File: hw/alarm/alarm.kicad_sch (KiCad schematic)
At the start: 64 parts, among them IC3 SHT40-BD1B-R2, IC5 PEC11S-929K-S0015, IC6 MAX31328NELB+, J1 4328, J2 FFC2B35-24-T, J3 975, Q1 DMG2305UX-7, Q2 2SC5585TL, Q3 Si1308EDL-T1-GE3, Q4 DMG2305UX-7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

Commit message: Finish most of board layout
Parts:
- removed S7: DS01-254-L-01BE, DS01254L01BE, symbol SamacSys_Parts:DS01-254-L-01BE
- added S7: RKB2SJK250SMTR_LFS, RKB2SJK250SMTRLFS, symbol SamacSys_Parts:RKB2SJK250SMTR_LFS
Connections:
- net +3.3V: now also S7.2 (COM_2)
- net Buzzer: now also U1.4 (GPIO2); no longer U1.20 (GPIO15)
- net EinkBUSY: now also U1.21 (GPIO16); no longer U1.22 (GPIO17)
- net EinkCS: now also U1.29 (GPIO22); no longer U1.10 (GPIO7)
- net EinkRESET: now also U1.22 (GPIO17); no longer U1.21 (GPIO16)
- net Enc_A1: now also U1.2 (GPIO1); no longer U1.11 (GPIO8)
- net Enc_B1: now also U1.1 (GPIO0); no longer U1.12 (GPIO9)
- net RF1: now also U1.20 (GPIO15); no longer U1.5 (GPIO3)
- net MISO: no longer names the net of U1.26 (GPIO20)
- net RF_key: no longer names the net of A1.7 (KEY), R15.2, R3.1
- net RF_key: now also S7.4 (NO_2); no longer U1.4 (GPIO2)
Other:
- note added: "Qwiic"
- note removed: "Stemma-QT"
- moved on the sheet: J1, R5, R6

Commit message: Finish board layout pending last checks
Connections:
- net GND: now also J3.3 (-); no longer J3.1 (-)
- net at Q4.3 (D): now also J3.1 (+); no longer J3.3 (+)
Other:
- moved on the sheet: J3
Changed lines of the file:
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@@
 	(wire
 		(pts
-			(xy 191.77 73.66) (xy 184.15 73.66)
-		)
-		(stroke
-			(width 0)
-			(type default)
-		)
-	)
-	(wire
-		(pts
 			(xy 396.24 175.26) (xy 403.86 175.26)
 		)
@@
 	(wire
 		(pts
-			(xy 191.77 73.66) (xy 191.77 74.93)
+			(xy 158.75 73.66) (xy 173.99 73.66)
 		)
 		(stroke
@@
 	(wire
 		(pts
-			(xy 186.69 278.13) (xy 194.31 278.13)
+			(xy 179.07 73.66) (xy 179.07 74.93)
 		)
 		(stroke
@@
 	(wire
 		(pts
-			(xy 179.07 73.66) (xy 179.07 74.93)
+			(xy 186.69 278.13) (xy 194.31 278.13)
 		)
 		(stroke
@@
 	(symbol
 		(lib_id "SamacSys_Parts:975")
-		(at 179.07 73.66 90)
+		(at 173.99 73.66 90)
 		(unit 1)
 		(exclude_from_sim no)
@@
 		(fields_autoplaced yes)
 		(property "Reference" "J3"
-			(at 187.96 62.2299 90)
+			(at 182.88 62.2299 90)
 			(effects
 				(font
@@
 		)
 		(property "Value" "975"
-			(at 187.96 64.7699 90)
+			(at 182.88 64.7699 90)
 			(effects
 				(font
@@
 		)
 		(property "Footprint" "975"
-			(at 273.99 57.15 0)
+			(at 268.91 57.15 0)
 			(effects
 				(font
@@
 		)
 		(property "Datasheet" "https://componentsearchengine.com/Datasheets/1/975.pdf"
-			(at 373.99 57.15 0)
+			(at 368.91 57.15 0)
 			(effects
 				(font
@@
 		)
 		(property "Description" "Headers & Wire Housings WIRE TO BOARD THM CONN, 3 TERM, VERT"
-			(at 179.07 73.66 0)
+			(at 173.99 73.66 0)
 			(effects
 				(font
@@
 		)
 		(property "Height" "7.7"
-			(at 573.99 57.15 0)
+			(at 568.91 57.15 0)
 			(effects
 				(font
@@
 		)
 		(property "Mouser Part Number" "534-975"
-			(at 673.99 57.15 0)
+			(at 668.91 57.15 0)
 			(effects
 				(font
@@
 		)
 		(property "Mouser Price/Stock" "https://www.mouser.co.uk/ProductDetail/Keystone-Electronics/975?qs=5aG0NVq1C4xEu03Xxaum1g%3D%3D"
-			(at 773.99 57.15 0)
+			(at 768.91 57.15 0)
 			(effects
 				(font
@@
 		)
 		(property "Manufacturer_Name" "Keystone Electronics"
-			(at 873.99 57.15 0)
+			(at 868.91 57.15 0)
 			(effects
 				(font
@@
 		)
 		(property "Manufacturer_Part_Number" "975"
-			(at 973.99 57.15 0)
+			(at 968.91 57.15 0)
 			(effects
 				(font
@@
 	(symbol
 		(lib_id "power:GND")
-		(at 191.77 74.93 0)
+		(at 158.75 73.66 270)
 		(unit 1)
 		(exclude_from_sim no)
@@
 		(fields_autoplaced yes)
 		(property "Reference" "#PWR019"
-			(at 191.77 81.28 0)
+			(at 152.4 73.66 0)
 			(effects
 				(font
@@
 		)
 		(property "Value" "GND"
-			(at 191.77 80.01 0)
+			(at 153.67 73.66 0)
 			(effects
 				(font
@@
 		)
 		(property "Footprint" ""
-			(at 191.77 74.93 0)
+			(at 158.75 73.66 0)
 			(effects
 				(font
@@
 		)
 		(property "Datasheet" ""
-			(at 191.77 74.93 0)
+			(at 158.75 73.66 0)
 			(effects
 				(font
@@
 		)
 		(property "Description" "Power symbol creates a global label with name \"GND\" , ground"
-			(at 191.77 74.93 0)
+			(at 158.75 73.66 0)
 			(effects
 				(font

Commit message: Further tweaks & corrections, create production files
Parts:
- removed IC5: PEC11S-929K-S0015, PEC11S929KS0015, symbol SamacSys_Parts:PEC11S-929K-S0015
- removed J1: 4328, 4328:ADAFRUIT_4328, symbol 4328:4328
- added H1, H2, H3, H4: MountingHole_Pad, MountingHole:MountingHole_2.7mm_M2.5_DIN965_Pad, symbol Mechanical:MountingHole_Pad
- added J4: SM04B-SRSS-TB_LF__SN__P_, SM04BSRSSTBLFSNP, symbol SamacSys_Parts:SM04B-SRSS-TB_LF__SN__P_
- added U2: PEC11R-4215F-S0024, PEC11R4215FS0024, symbol SamacSys_Parts:PEC11R-4215F-S0024
- D1, D3, D4, D5: LCSC Part # (none) -> C77336
- IC3: LCSC Part # (none) -> C7461849
- IC6: LCSC Part # (none) -> C3303818
- J2: LCSC Part # (none) -> C5641278
- LS2: LCSC Part # (none) -> C7116026
- Q1, Q4: LCSC Part # (none) -> C150470
- Q2: LCSC Part # (none) -> C337983
- Q3: LCSC Part # (none) -> C469327
- S1, S7: LCSC Part # (none) -> C2927789
- S2, S3, S4, S5, S6, S8, S9: LCSC Part # (none) -> C2689517
- U4: LCSC Part # (none) -> C2649434
- U5: LCSC Part # (none) -> C7067210
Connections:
- net +3.3V: now also J4.3
- net DC: now also U1.29 (GPIO22); no longer U1.27 (GPIO21)
- net EinkCS: now also U1.27 (GPIO21); no longer U1.29 (GPIO22)
- net Enc_D: now also U2.1 (COM)
- net Enc_E: now also U2.2 (NO)
- net GND: now also H1.1, H2.1, H3.1, H4.1, J4.4, U2.C1 (COMMON)
- net RTC_INT: now also U1.14 (GPIO10); no longer U1.19 (GPIO14)
- net SCL: now also J4.1
- net SDA: now also J4.2
- net at C19.2, R11.2, R9.2: now also U2.A1 (CHANNEL_A)
- net at C18.2, R10.1, R12.2: now also U2.B1 (CHANNEL_B)
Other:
- moved on the sheet: C18, C19, J3, Q4, R10, R11, R12, R9

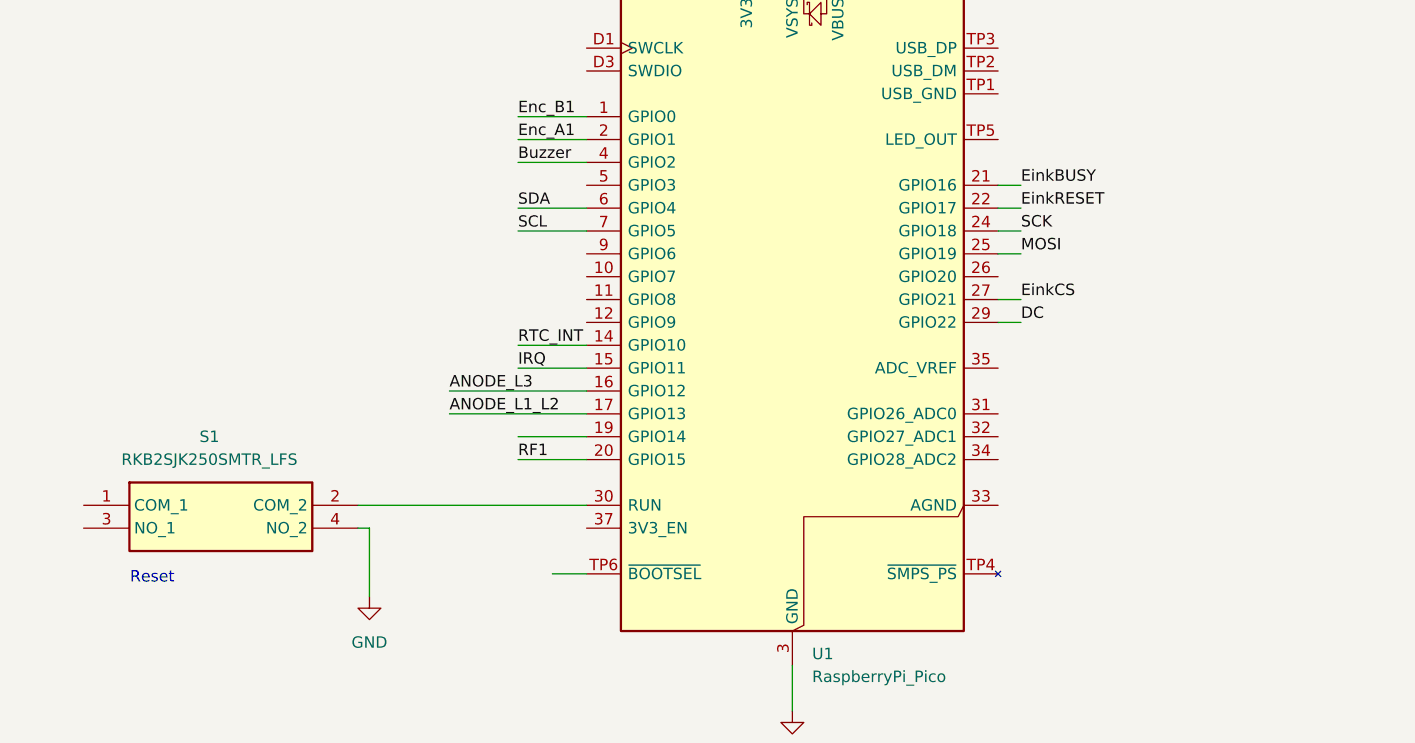
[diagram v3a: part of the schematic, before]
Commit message: Add connectors for unused pins
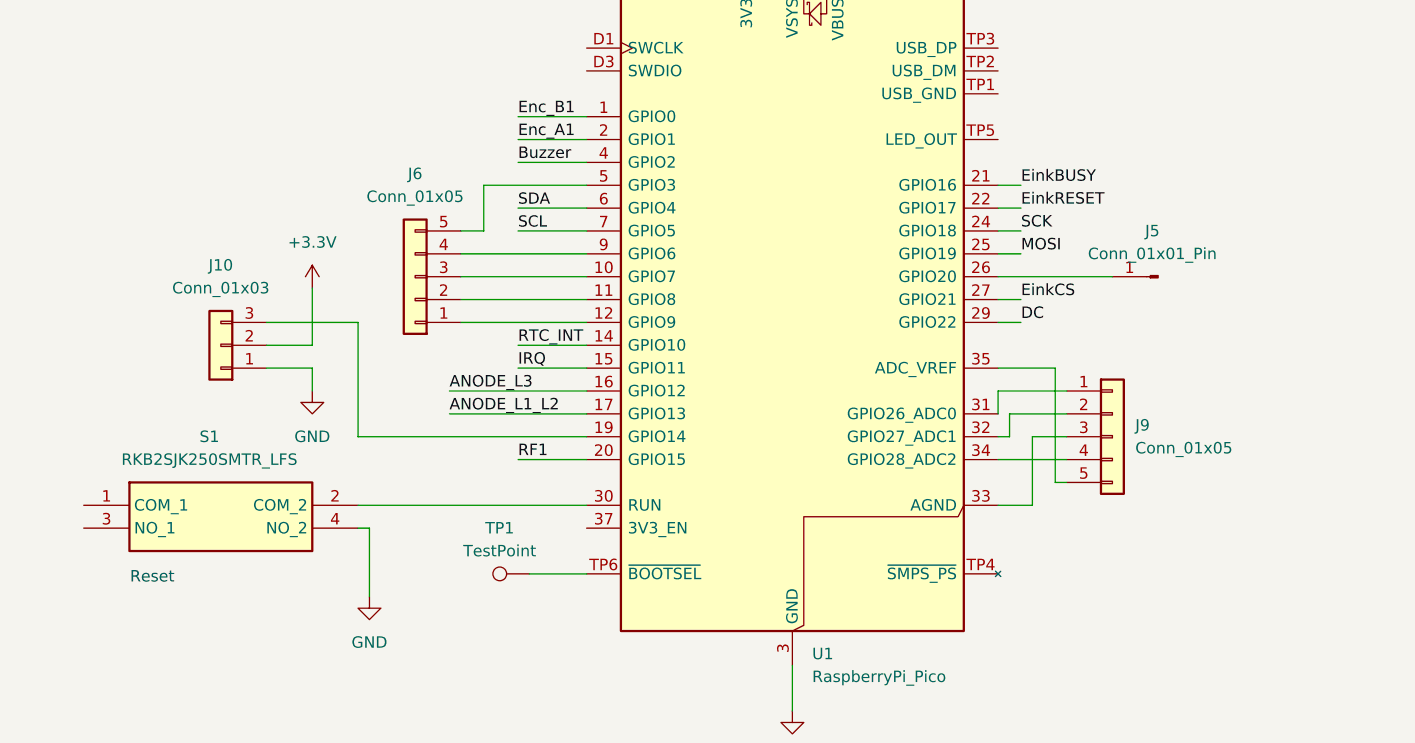
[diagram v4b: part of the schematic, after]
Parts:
- added J10: Conn_01x03, Connector_PinHeader_2.54mm:PinHeader_1x03_P2.54mm_Vertical, symbol Connector_Generic:Conn_01x03
- added J5: Conn_01x01_Pin, Connector_PinHeader_2.54mm:PinHeader_1x01_P2.54mm_Vertical, symbol Connector:Conn_01x01_Pin
- added J6, J9: Conn_01x05, Connector_PinHeader_2.54mm:PinHeader_1x05_P2.54mm_Vertical, symbol Connector_Generic:Conn_01x05
- added TP1: TestPoint, TestPoint:TestPoint_Pad_D1.5mm, symbol Connector:TestPoint
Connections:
- net +3.3V: now also J10.2 (Pin_2)
- net GND: now also J10.1 (Pin_1)
- net at U1.10 (GPIO7): now also J6.3 (Pin_3)
- net at U1.11 (GPIO8): now also J6.2 (Pin_2)
- net at U1.12 (GPIO9): now also J6.1 (Pin_1)
- net at U1.19 (GPIO14): now also J10.3 (Pin_3)
- net at U1.26 (GPIO20): now also J5.1 (Pin_1)
- net at U1.31 (GPIO26_ADC0): now also J9.1 (Pin_1)
- net at U1.32 (GPIO27_ADC1): now also J9.2 (Pin_2)
- net at U1.33 (AGND): now also J9.3 (Pin_3)
- net at U1.34 (GPIO28_ADC2): now also J9.4 (Pin_4)
- net at U1.35 (ADC_VREF): now also J9.5 (Pin_5)
- net at U1.5 (GPIO3): now also J6.5 (Pin_5)
- net at U1.9 (GPIO6): now also J6.4 (Pin_4)
- net at U1.TP6 (~{BOOTSEL}): now also TP1.1

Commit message: Add LCSC PNs, Replace through-hole breakouts with SMD header, reannotate
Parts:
- removed J10: Conn_01x03, Connector_PinHeader_2.54mm:PinHeader_1x03_P2.54mm_Vertical, symbol Connector_Generic:Conn_01x03
- removed J3: 975, 975, symbol SamacSys_Parts:975
- removed J5: Conn_01x01_Pin, Connector_PinHeader_2.54mm:PinHeader_1x01_P2.54mm_Vertical, symbol Connector:Conn_01x01_Pin
- removed J6, J9: Conn_01x05, Connector_PinHeader_2.54mm:PinHeader_1x05_P2.54mm_Vertical, symbol Connector_Generic:Conn_01x05
- removed Q1, Q4: DMG2305UX-7, SOT96P240X115-3N, symbol SamacSys_Parts:DMG2305UX-7
- added J2: 975, SamacSys_Parts:975, symbol SamacSys_Parts:975
- added J3: M20-7920642R, SamacSys_Parts:M207920642R, symbol SamacSys_Parts:M20-7920642R
- added Q2, Q3: DMG2305UX-7, SamacSys_Parts:SOT96P240X115-3N, symbol SamacSys_Parts:DMG2305UX-7
- added TP1, TP3: TestPoint, TestPoint:TestPoint_Pad_1.5x1.5mm, symbol Connector:TestPoint
- C1: renamed from C16; LCSC Part # (none) -> C8032
- C10: renamed from C5; LCSC Part # (none) -> C105524
- C11: renamed from C3; LCSC Part # (none) -> C105524
- C12: renamed from C7; LCSC Part # (none) -> C105524
- C13: renamed from C2; LCSC Part # (none) -> C105524
- C14: renamed from C19; LCSC Part # (none) -> C105524
- C15: renamed from C18; LCSC Part # (none) -> C105524
- C16: renamed from C15; LCSC Part # (none) -> C105524
- C17: LCSC Part # (none) -> C105524
- C18: renamed from C1; LCSC Part # (none) -> C8032
- C2: renamed from C11; LCSC Part # (none) -> C105524
- C3: renamed from C12; LCSC Part # (none) -> C8032
- C4: renamed from C13; LCSC Part # (none) -> C105524
- C5: renamed from C9; LCSC Part # (none) -> C105524
- C6: renamed from C10; LCSC Part # (none) -> C8032
- C7: renamed from C6; LCSC Part # (none) -> C105524
- C8: renamed from C4; LCSC Part # (none) -> C105524
- C9: renamed from C8; LCSC Part # (none) -> C105524
- IC1: renamed from IC3; footprint SHT40BD1BR2 -> SamacSys_Parts:SHT40BD1BR2
- IC2: renamed from IC6; footprint MAX31328NELB -> SamacSys_Parts:MAX31328NELB
- J1: renamed from J2; footprint FFC2B3524T -> SamacSys_Parts:FFC2B3524T
- J4: footprint SM04BSRSSTBLFSNP -> SamacSys_Parts:SM04BSRSSTBLFSNP
- L1: footprint INDM3225X240N -> SamacSys_Parts:INDM3225X240N; LCSC Part # (none) -> C1499398
- LS1: renamed from LS2; footprint CSSI4B20SMTTR -> SamacSys_Parts:CSSI4B20SMTTR
- Q1: renamed from Q3; footprint SOT65P210X110-3N -> SamacSys_Parts:SOT65P210X110-3N
- Q4: renamed from Q2; footprint 2SC5585TL -> SamacSys_Parts:2SC5585TL
- R1: renamed from R2; LCSC Part # (none) -> C15401
- R10: renamed from R5; LCSC Part # (none) -> C15401
- R11: renamed from R8; LCSC Part # (none) -> C15401
- R12: renamed from R4; value 13.9kΩ -> 14kΩ; LCSC Part # (none) -> C137795
- R13: renamed from R3; LCSC Part # (none) -> C103198
- R14: renamed from R15; LCSC Part # (none) -> C1211
- R15: renamed from R13; LCSC Part # (none) -> C22796
- R16: renamed from R7; LCSC Part # (none) -> C22796
- R2: renamed from R1; LCSC Part # (none) -> C23411
- R3: renamed from R11; LCSC Part # (none) -> C15401
- R4: renamed from R12; LCSC Part # (none) -> C15401
- R5: renamed from R14; LCSC Part # (none) -> C15401
- R6: renamed from R16; LCSC Part # (none) -> C100819
- R7: renamed from R9; LCSC Part # (none) -> C15401
- R8: renamed from R10; LCSC Part # (none) -> C15401
- R9: renamed from R6; LCSC Part # (none) -> C15401
- S1: footprint RKB2SJK250SMTRLFS -> SamacSys_Parts:RKB2SJK250SMTRLFS
- S2: renamed from S7; footprint RKB2SJK250SMTRLFS -> SamacSys_Parts:RKB2SJK250SMTRLFS
- S3: renamed from S5; footprint PTS647SM38SMTR2LFS -> SamacSys_Parts:PTS647SM38SMTR2LFS
- S4, S8, S9: footprint PTS647SM38SMTR2LFS -> SamacSys_Parts:PTS647SM38SMTR2LFS
- S5: renamed from S3; footprint PTS647SM38SMTR2LFS -> SamacSys_Parts:PTS647SM38SMTR2LFS
- S6: renamed from S2; footprint PTS647SM38SMTR2LFS -> SamacSys_Parts:PTS647SM38SMTR2LFS
- S7: renamed from S6; footprint PTS647SM38SMTR2LFS -> SamacSys_Parts:PTS647SM38SMTR2LFS
- TP2: renamed from TP1; footprint TestPoint:TestPoint_Pad_D1.5mm -> TestPoint:TestPoint_Pad_1.5x1.5mm
- U2: footprint PEC11R4215FS0024 -> SamacSys_Parts:PEC11R4215FS0024
- U4: renamed from U5; footprint TDCG1060M_VIS -> footprints:TDCG1060M_VIS
- renumbered D3 to D1, D4 to D2, D5 to D3, D1 to D4, D2 to D5, U4 to U3
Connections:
- net +3.3V: now also J3.1
- net GND: now also J2.3 (-), J3.2, Q2.1 (G)
- net RTC_INT: now also U1.5 (GPIO3); no longer U1.14 (GPIO10)
- net GP9: now reaches U1.12 (GPIO9)
- net GP9: now also J3.5
- net GP8: now reaches U1.11 (GPIO8)
- net GP8: now also J3.7
- net GP7: now reaches U1.10 (GPIO7)
- net GP7: now also J3.9
- net GP6: now reaches U1.9 (GPIO6)
- net GP6: now also J3.11
- net at U1.26 (GPIO20): now also TP3.1
- net at U1.19 (GPIO14): now also TP1.1
- net ADC0: now reaches U1.31 (GPIO26_ADC0)
- net ADC0: now also J3.4
- net ADC1: now reaches U1.32 (GPIO27_ADC1)
- net ADC1: now also J3.6
- net AGND: now reaches U1.33 (AGND)
- net AGND: now also J3.8
- net ADC2: now reaches U1.34 (GPIO28_ADC2)
- net ADC2: now also J3.10
- net ADC_VREF: now reaches U1.35 (ADC_VREF)
- net ADC_VREF: now also J3.12
- net VSYS: now reaches U1.39 (VSYS)
- net VSYS: now also Q3.2 (S)
- net VBUS: now reaches U1.40 (VBUS)
- net VBUS: now also Q3.1 (G)
- new net: Q2.2 (S), Q3.3 (D)
- new net: J2.1 (+), Q2.3 (D)
- new net GP14: J3.3, U1.14 (GPIO10)
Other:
- note added: "IO Breakout"
- note added: "Mounting"
- note added: "Power"
- moved on the sheet: H1, H2, H3, H4, S1, TP2, U1

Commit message: Start work on v3.0
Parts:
- removed S3, S4, S5, S6, S7, S8, S9: PTS647SM70SMTR2LFS, SamacSys_Parts:PTS647SM38SMTR2LFS, symbol SamacSys_Parts:PTS647SM70SMTR2LFS
- removed U2: PEC11R-4215F-S0024, SamacSys_Parts:PEC11R4215FS0024, symbol SamacSys_Parts:PEC11R-4215F-S0024
- added IC3: PEC11S-929K-S0015, PEC11S929KS0015, symbol SamacSys_Parts:PEC11S-929K-S0015
- added S3, S4, S5, S7, S8, S9: TL3301BF260QJ, TL3301BF260QJ, symbol SamacSys_Parts:TL3301BF260QJ
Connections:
- net +3.3V: no longer R13.2
- net Enc_D: now also IC3.D1 (COM), S3.4, S4.4, S5.4, S7.4, S8.4, S9.4
- net Enc_E: now also IC3.E1 (NO)
- net GND: now also IC3.C1 (WIPER)
- net at C14.2, R3.2, R7.2: now also IC3.A1 (CCW)
- net at U3.15 (SEGA), U4.14 (ANODE_A): now also S3.3
- net at U3.16 (SEGF), U4.11 (ANODE_F): now also S8.1
- net at C15.2, R4.2, R8.1: now also IC3.B1 (CW)
- net at U3.17 (SEGB), U4.16 (ANODE_B): now also S4.1
- net at U3.21 (SEGE), U4.5 (ANODE_E): now also S7.1
- net at U3.18 (SEGG), U4.15 (ANODE_G): now also S9.1
- net at U3.20 (SEGC), U4.13 (ANODE_C): now also S5.1
- net at A1.7 (KEY), R13.1, R14.2: no longer S2.4 (NO_2)
- new net: R13.2, S2.4 (NO_2)
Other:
- moved on the sheet: R13
